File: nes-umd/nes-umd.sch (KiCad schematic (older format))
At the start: 4 parts, among them CON101 NES-CONN, CON102 UMD-CONN

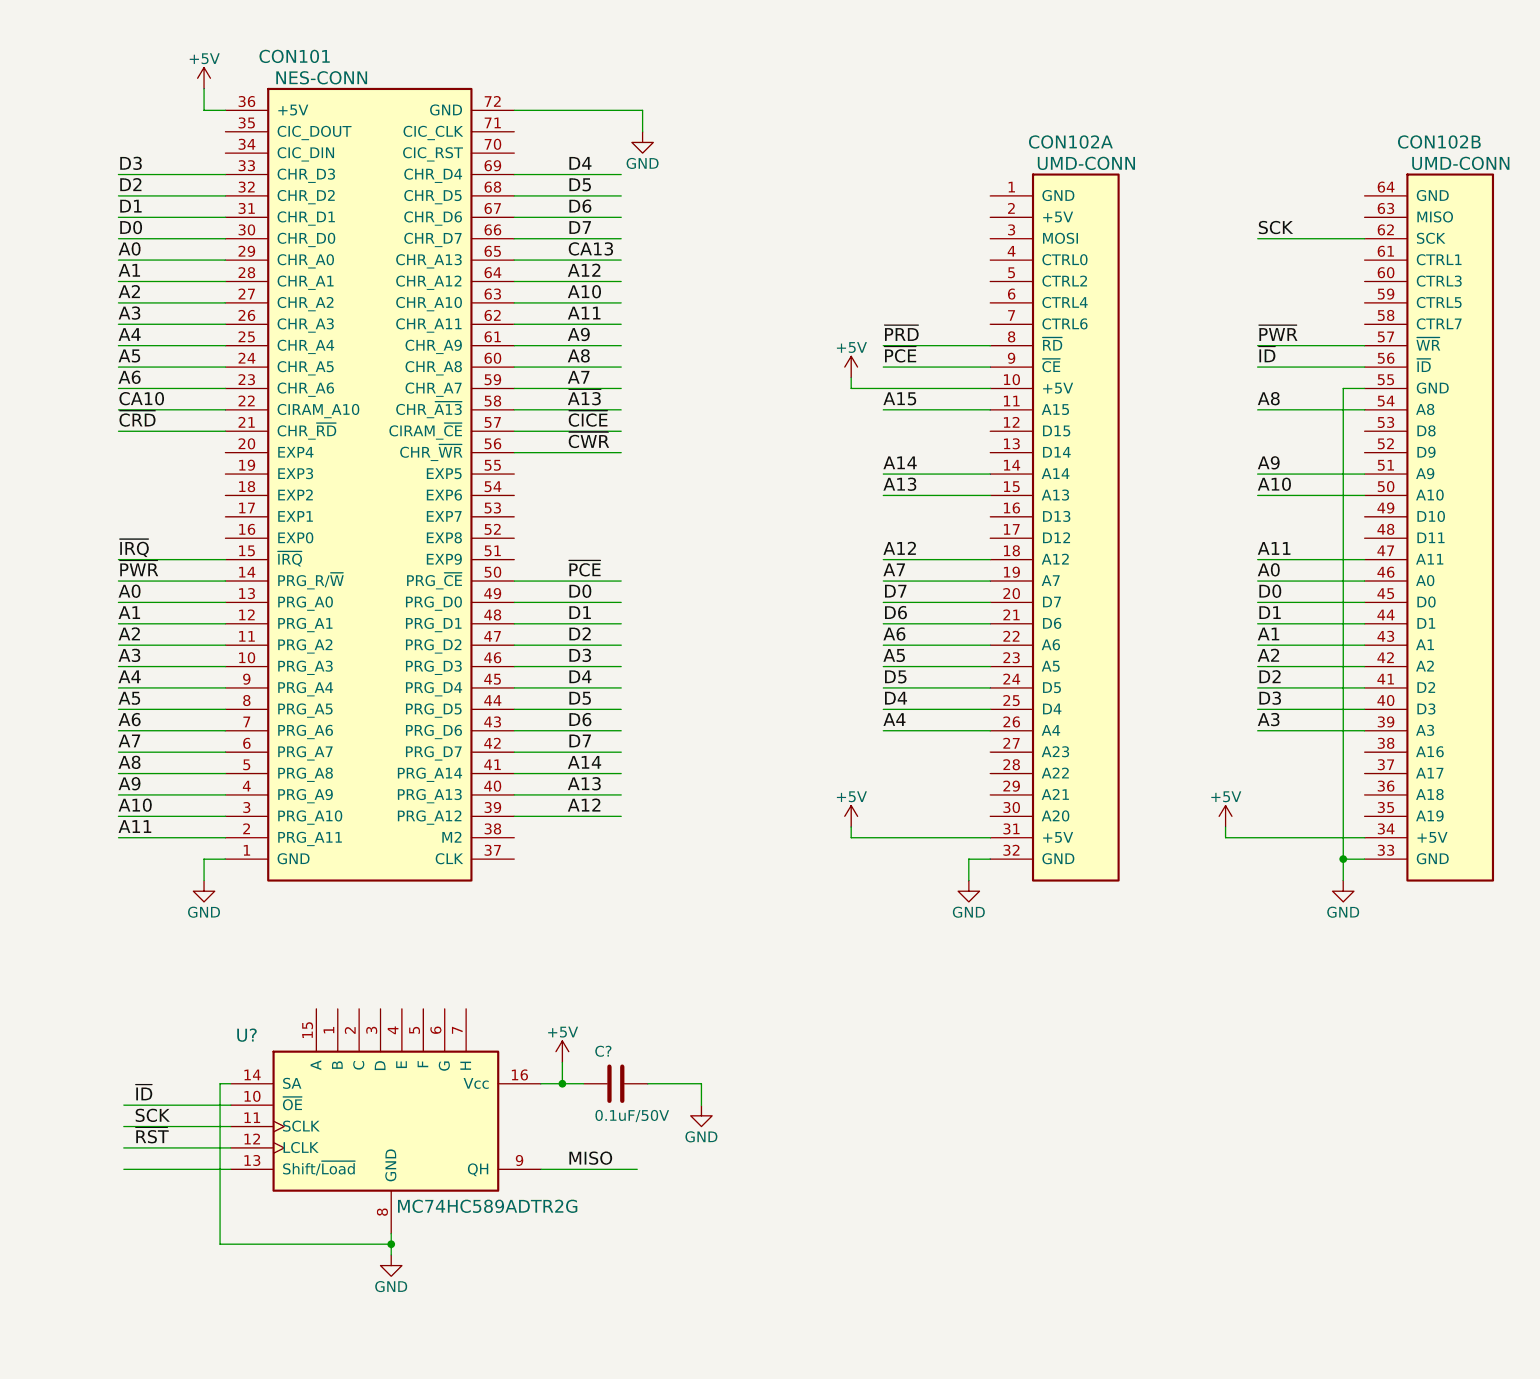
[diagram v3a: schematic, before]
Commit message: saved 1 pin on the ID function
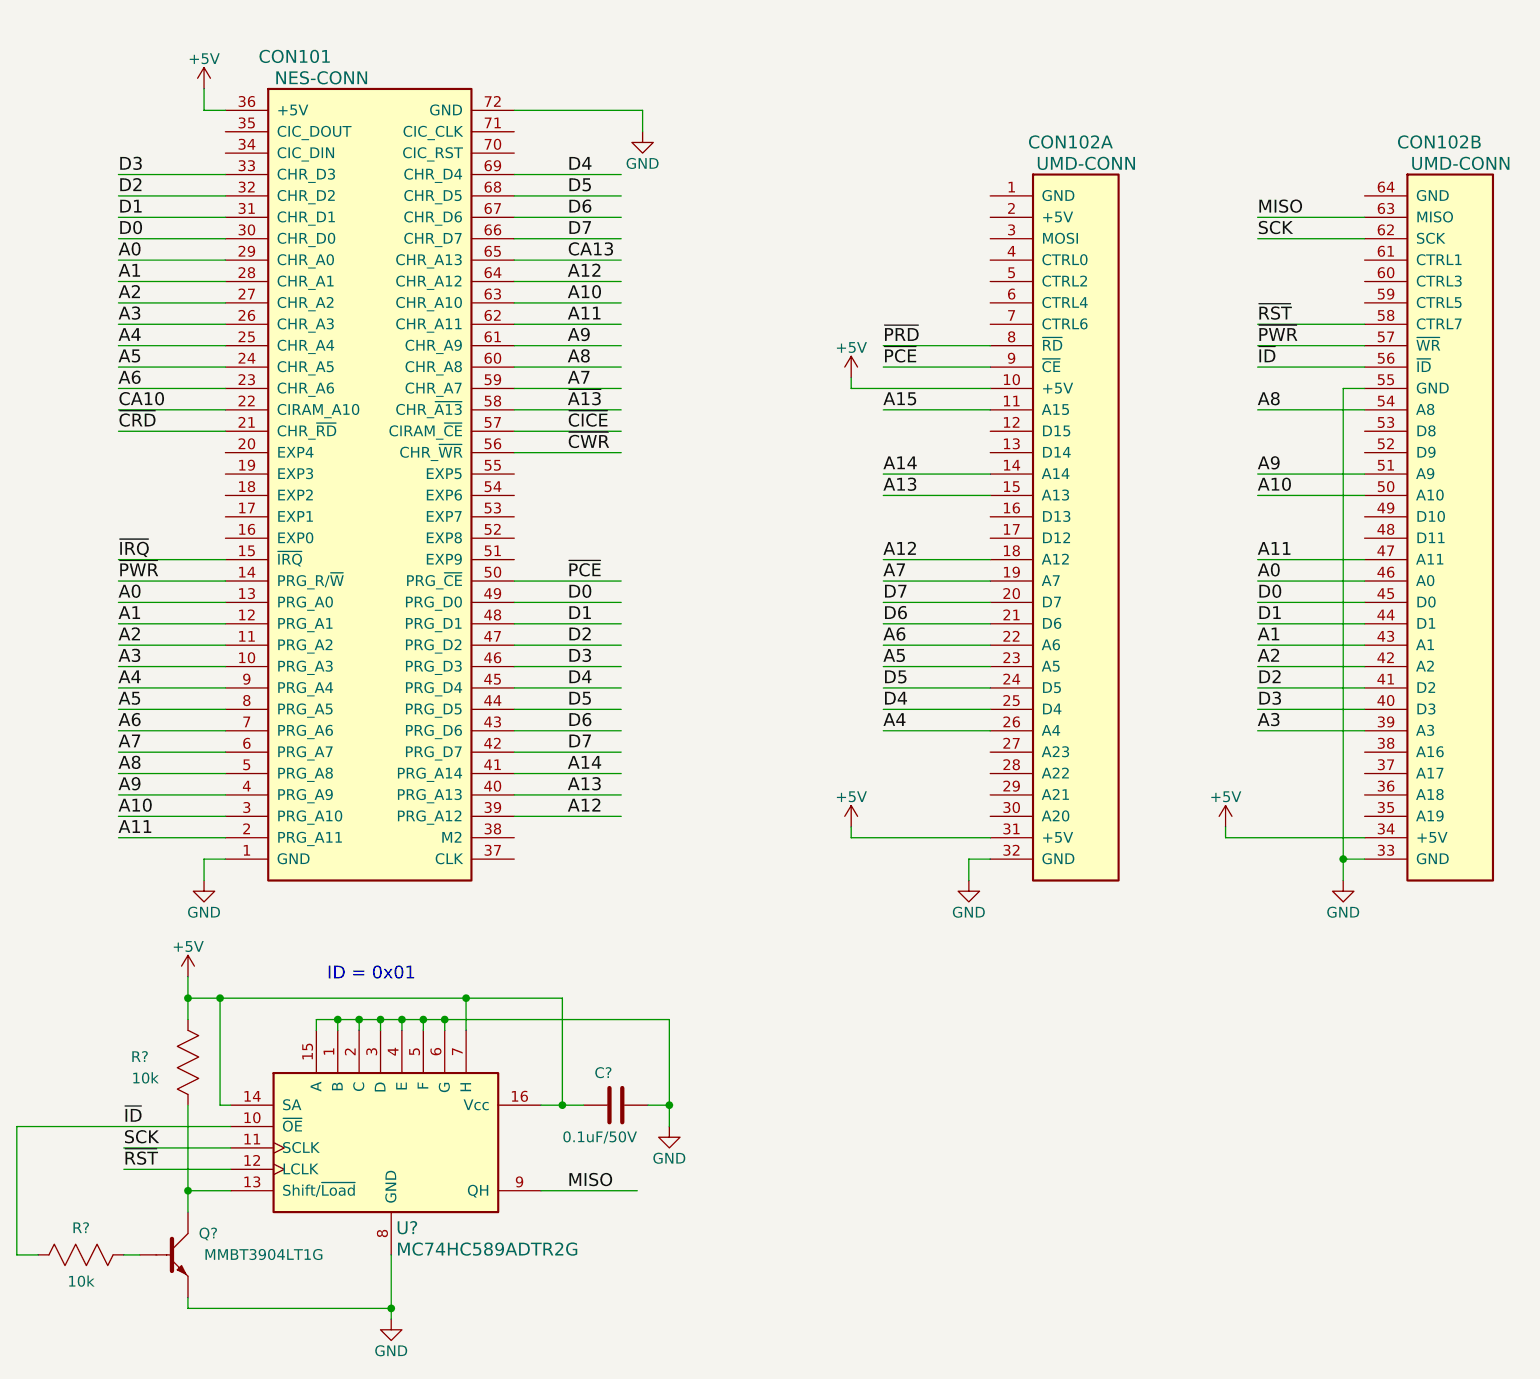
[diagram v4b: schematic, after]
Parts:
- added Q?: MMBT3904LT1G, SOT-23, symbol MMBT3904LT1G
- added R? (x2): 10k, db-smt:0603, symbol R_0603
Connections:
- wire segments 112 -> 144
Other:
- note added: "ID = 0x01"
- moved on the sheet: C?, U?
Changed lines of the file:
@@
 	8050 5400 7950 5400
 Wire Wire Line
-	7950 3200 7950 5500
+	7950 3200 7950 5400
+Wire Wire Line
+	7950 5400 7950 5500
 Wire Wire Line
 	6300 5400 6200 5400
@@
 L MC74HC589ADTR2G U?
 U 1 1 5AB17DEA
-P 2950 6300
-F 0 "U?" H 2825 6375 60  0000 C CNN
+P 2950 6400
+F 0 "U?" H 3575 5675 60  0000 C CNN
 F 1 "MC74HC589ADTR2G" H 3950 5575 60  0000 C CNN
-F 2 "db-smt:TSSOP-16" H 3425 7000 60  0001 C CNN
-F 3 "http://www.onsemi.com/pub/Collateral/MC74HC589A-D.PDF" H 4400 6900 60  0001 C CNN
-F 4 "MC74HC589ADTR2GOSCT-ND" H 3650 6800 60  0001 C CNN "Digikey"
-F 5 "IC SHIFT REGISTER 8BIT 16-TSSOP" H 3800 6700 60  0001 C CNN "Description"
-	1    2950 6300
+F 2 "db-smt:TSSOP-16" H 3425 7100 60  0001 C CNN
+F 3 "http://www.onsemi.com/pub/Collateral/MC74HC589A-D.PDF" H 4400 7000 60  0001 C CNN
+F 4 "MC74HC589ADTR2GOSCT-ND" H 3650 6900 60  0001 C CNN "Digikey"
+F 5 "IC SHIFT REGISTER 8BIT 16-TSSOP" H 3800 6800 60  0001 C CNN "Description"
+	1    2950 6400
 	1    0    0    -1
 $EndComp
@@
 L GND #PWR?
 U 1 1 5AB17ED4
-P 3500 7250
-F 0 "#PWR?" H 3500 7000 50  0001 C CNN
-F 1 "GND" H 3500 7100 50  0000 C CNN
-F 2 "" H 3500 7250 50  0001 C CNN
-F 3 "" H 3500 7250 50  0001 C CNN
-	1    3500 7250
+P 3500 7550
+F 0 "#PWR?" H 3500 7300 50  0001 C CNN
+F 1 "GND" H 3500 7400 50  0000 C CNN
+F 2 "" H 3500 7550 50  0001 C CNN
+F 3 "" H 3500 7550 50  0001 C CNN
+	1    3500 7550
 	1    0    0    -1
 $EndComp
 Wire Wire Line
-	3500 7150 3500 7250
-Wire Wire Line
-	4200 6850 4650 6850
-Text Label 4325 6850 0    60   ~ 0
+	4200 6950 4650 6950
+Text Label 4325 6950 0    60   ~ 0
 MISO
 Wire Wire Line
-	2750 6650 2250 6650
-Wire Wire Line
-	2250 6550 2750 6550
-Wire Wire Line
 	2750 6750 2250 6750
 Wire Wire Line
+	1750 6650 2750 6650
+Wire Wire Line
 	2750 6850 2250 6850
 Wire Wire Line
-	2750 6450 2700 6450
-Wire Wire Line
-	2700 6450 2700 7200
-Wire Wire Line
-	2700 7200 3500 7200
-Connection ~ 3500 7200
-Text Label 2300 6550 0    60   ~ 0
+	2750 6550 2700 6550
+Text Label 2250 6650 0    60   ~ 0
 ~ID
-Text Label 2300 6650 0    60   ~ 0
+Text Label 2250 6750 0    60   ~ 0
 SCK
-Text Label 2300 6750 0    60   ~ 0
+Text Label 2250 6850 0    60   ~ 0
 ~RST
-$Comp
-L +5V #PWR?
-U 1 1 5AB199F3
-P 4300 6350
-F 0 "#PWR?" H 4300 6200 50  0001 C CNN
-F 1 "+5V" H 4300 6490 50  0000 C CNN
-F 2 "" H 4300 6350 50  0001 C CNN
-F 3 "" H 4300 6350 50  0001 C CNN
-	1    4300 6350
-	1    0    0    -1
-$EndComp
 $Comp
 L C_0603 C?
 U 1 1 5AB1A108
-P 4550 6450
-F 0 "C?" V 4400 6350 50  0000 L CNN
-F 1 "0.1uF/50V" V 4700 6350 50  0000 L CNN
-F 2 "db-smt:0603" H 5050 6350 30  0001 C CNN
-F 3 "" H 4575 6550 60  0001 C CNN
-F 4 "#ND" H 4975 6425 60  0001 C CNN "Digikey"
-F 5 "#ND" H 4975 6525 60  0001 C CNN "Description"
-	1    4550 6450
+P 4550 6550
+F 0 "C?" V 4400 6450 50  0000 L CNN
+F 1 "0.1uF/50V" V 4700 6300 50  0000 L CNN
+F 2 "db-smt:0603" H 5050 6450 30  0001 C CNN
+F 3 "" H 4575 6650 60  0001 C CNN
+F 4 "#ND" H 4975 6525 60  0001 C CNN "Digikey"
+F 5 "#ND" H 4975 6625 60  0001 C CNN "Description"
+	1    4550 6550
 	0    1    1    0
 $EndComp
@@
 L GND #PWR?
 U 1 1 5AB1A4A7
-P 4950 6550
-F 0 "#PWR?" H 4950 6300 50  0001 C CNN
-F 1 "GND" H 4950 6400 50  0000 C CNN
-F 2 "" H 4950 6550 50  0001 C CNN
-F 3 "" H 4950 6550 50  0001 C CNN
-	1    4950 6550
+P 4800 6650
+F 0 "#PWR?" H 4800 6400 50  0001 C CNN
+F 1 "GND" H 4800 6500 50  0000 C CNN
+F 2 "" H 4800 6650 50  0001 C CNN
+F 3 "" H 4800 6650 50  0001 C CNN
+	1    4800 6650
 	1    0    0    -1
 $EndComp
 Wire Wire Line
-	4400 6450 4200 6450
-Wire Wire Line
-	4300 6350 4300 6450
-Connection ~ 4300 6450
-Wire Wire Line
-	4700 6450 4950 6450
-Wire Wire Line
-	4950 6450 4950 6550
+	4200 6550 4300 6550
+Wire Wire Line
+	4300 6550 4400 6550
+Wire Wire Line
+	4300 6050 4300 6550
+Connection ~ 4300 6550
+Wire Wire Line
+	4700 6550 4800 6550
+Wire Wire Line
+	4800 6150 4800 6550
+Wire Wire Line
+	4800 6550 4800 6650
 Wire Wire Line
 	8050 3100 7550 3100
@@
 Text Label 7550 2500 0    60   ~ 0
 SCK
+Wire Wire Line
+	7550 2900 8050 2900
+Text Label 7550 2900 0    60   ~ 0
+~RST
+$Comp
+L MMBT3904LT1G Q?
+U 1 1 5AB24199
+P 2450 7250
+F 0 "Q?" H 2600 7350 50  0000 L CNN
+F 1 "MMBT3904LT1G" H 2625 7250 50  0000 L CNN
+F 2 "SOT-23" H 2650 7175 50  0001 L CIN
+F 3 "" H 2450 7250 50  0000 L CNN
+	1    2450 7250
+	1    0    0    -1
+$EndComp
+Wire Wire Line
+	2750 6950 2550 6950
+Wire Wire Line
+	2550 6550 2550 6950
+Wire Wire Line
+	2550 6950 2550 7050
+Wire Wire Line
+	2550 7450 2550 7500
+Wire Wire Line
+	2550 7500 3500 7500
+Wire Wire Line
+	3500 7250 3500 7500
+Wire Wire Line
+	3500 7500 3500 7550
+Connection ~ 3500 7500
+$Comp
+L R_0603 R?
+U 1 1 5AB24683
+P 2050 7250
+F 0 "R?" V 1925 7250 50  0000 C CNN
+F 1 "10k" V 2175 7250 50  0000 C CNN
+F 2 "db-smt:0603" H 2350 7150 30  0001 C CNN
+F 3 "" H 2150 7250 30  0001 C CNN
+F 4 "P10.0KHCT-ND" H 2300 7225 60  0001 C CNN "Digikey"
+F 5 "RES SMD 10K OHM 1% 1/10W 0603" H 2300 7325 60  0001 C CNN "Description"
+	1    2050 7250
+	0    1    1    0
+$EndComp
+Wire Wire Line
+	2325 7250 2250 7250
+$Comp
+L R_0603 R?
+U 1 1 5AB24953
+P 2550 6350
+F 0 "R?" H 2775 6325 50  0000 C CNN
+F 1 "10k" H 2750 6425 50  0000 C CNN
+F 2 "db-smt:0603" H 2850 6250 30  0001 C CNN
+F 3 "" H 2650 6350 30  0001 C CNN
+F 4 "P10.0KHCT-ND" H 2800 6325 60  0001 C CNN "Digikey"
+F 5 "RES SMD 10K OHM 1% 1/10W 0603" H 2800 6425 60  0001 C CNN "Description"
+	1    2550 6350
+	-1   0    0    1
+$EndComp
+Connection ~ 2550 6950
+$Comp
+L +5V #PWR?
+U 1 1 5AB256F6
+P 2550 5950
+F 0 "#PWR?" H 2550 5800 50  0001 C CNN
+F 1 "+5V" H 2550 6090 50  0000 C CNN
+F 2 "" H 2550 5950 50  0001 C CNN
+F 3 "" H 2550 5950 50  0001 C CNN
+	1    2550 5950
+	1    0    0    -1
+$EndComp
+Wire Wire Line
+	2550 5950 2550 6050
+Wire Wire Line
+	2550 6050 2550 6150
+Wire Wire Line
+	2700 6550 2700 6050
+Wire Wire Line
+	2550 6050 2700 6050
+Wire Wire Line
+	2700 6050 3850 6050
+Wire Wire Line
+	3850 6050 4300 6050
+Connection ~ 2550 6050
+Wire Wire Line
+	1850 7250 1750 7250
+Wire Wire Line
+	1750 7250 1750 6650
+Wire Wire Line
+	3850 6050 3850 6200
+Connection ~ 2700 6050
+Connection ~ 3850 6050
+Wire Wire Line
+	8050 2400 7550 2400
+Text Label 7550 2400 0    60   ~ 0
+MISO
+Wire Wire Line
+	3150 6200 3150 6150
+Wire Wire Line
+	3150 6150 3250 6150
+Wire Wire Line
+	3250 6150 3350 6150
+Wire Wire Line
+	3350 6150 3450 6150
+Wire Wire Line
+	3450 6150 3550 6150
+Wire Wire Line
+	3550 6150 3650 6150
+Wire Wire Line
+	3650 6150 3750 6150
+Wire Wire Line
+	3750 6150 4800 6150
+Connection ~ 4800 6550
+Wire Wire Line
+	3250 6150 3250 6200
+Connection ~ 3250 6150
+Wire Wire Line
+	3350 6200 3350 6150
+Connection ~ 3350 6150
+Wire Wire Line
+	3450 6200 3450 6150
+Connection ~ 3450 6150
+Wire Wire Line
+	3550 6200 3550 6150
+Connection ~ 3550 6150
+Wire Wire Line
+	3650 6200 3650 6150
+Connection ~ 3650 6150
+Wire Wire Line
+	3750 6200 3750 6150
+Connection ~ 3750 6150
+Text Notes 3200 5975 0    60   ~ 0
+ID = 0x01
 $EndSCHEMATC

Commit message: parts placement for ID register
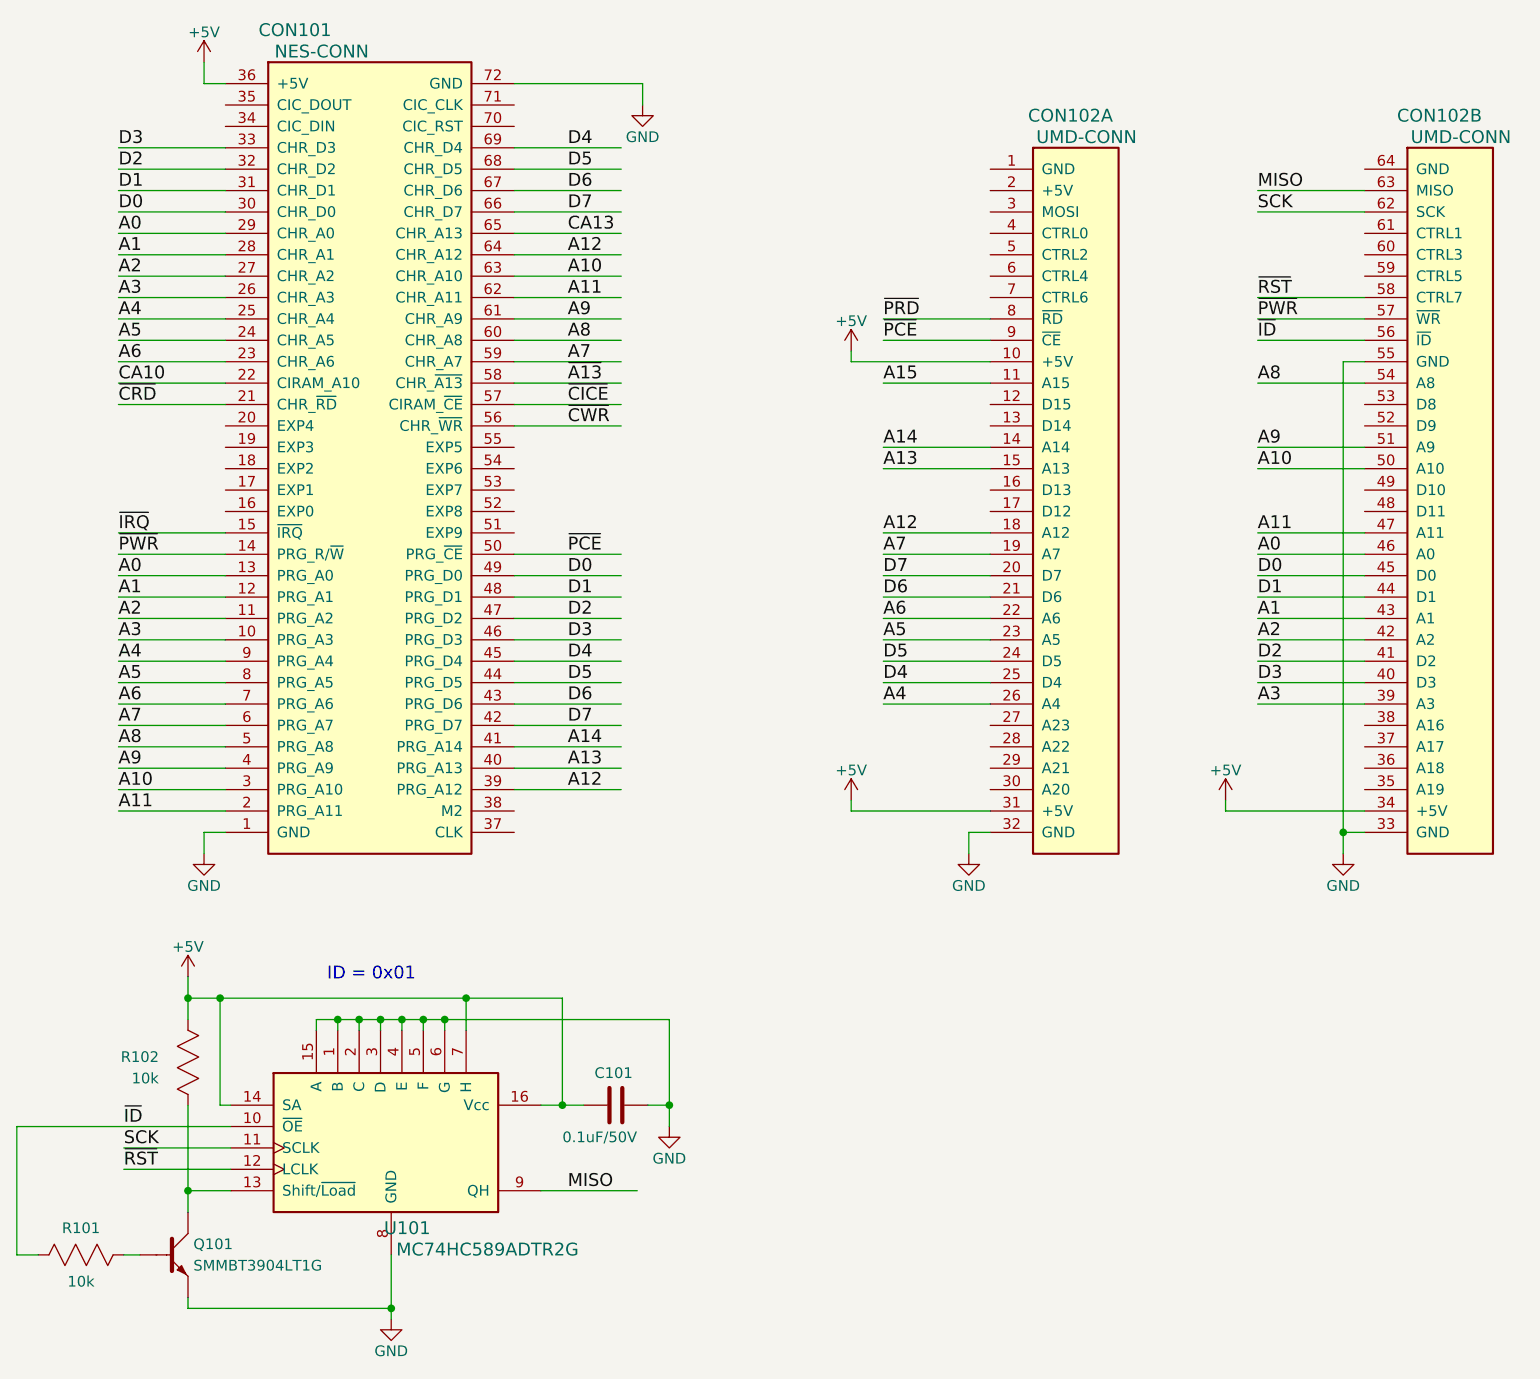
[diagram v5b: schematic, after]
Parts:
- removed Q?: MMBT3904LT1G, SOT-23, symbol MMBT3904LT1G
- added Q101: SMMBT3904LT1G, db-smt:SOT23, symbol SMMBT3904LT1G
- gave numbers to parts that had none: 4
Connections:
- wire segments 144 -> 130
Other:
- moved on the sheet: CON101, CON102A, CON102B
